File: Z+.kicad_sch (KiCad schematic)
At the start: 8 parts

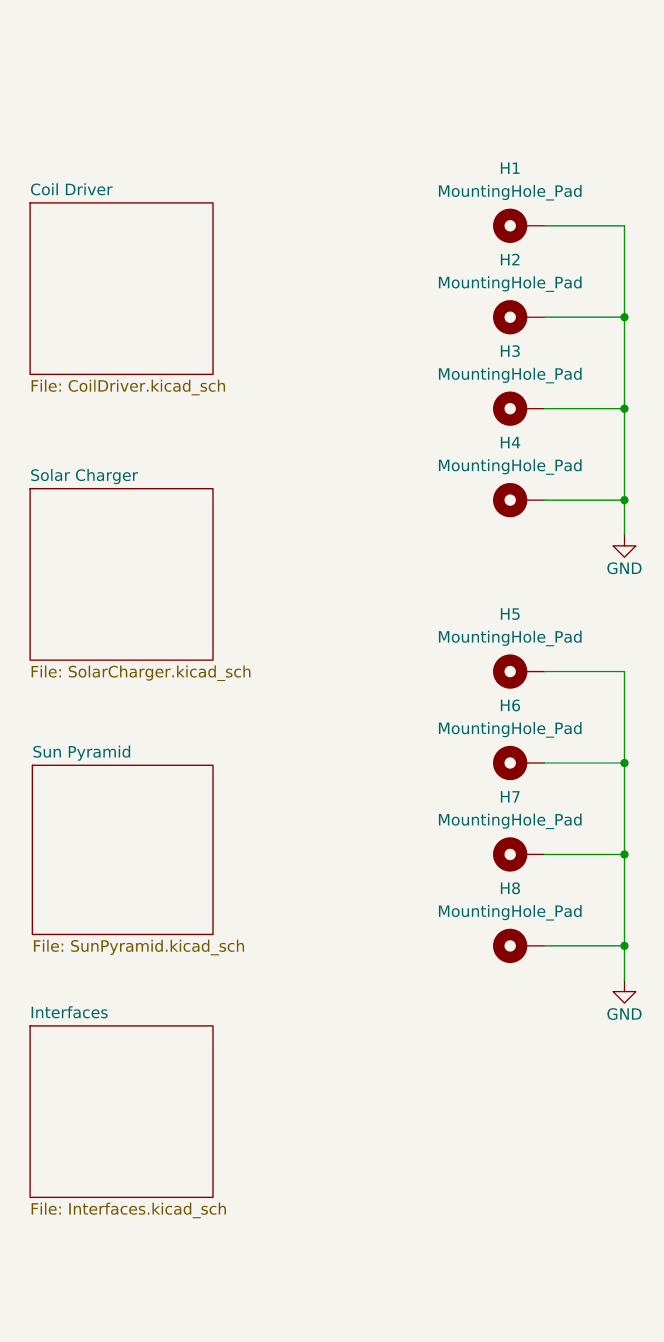
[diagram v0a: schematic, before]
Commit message: Cleaned up silkscreen
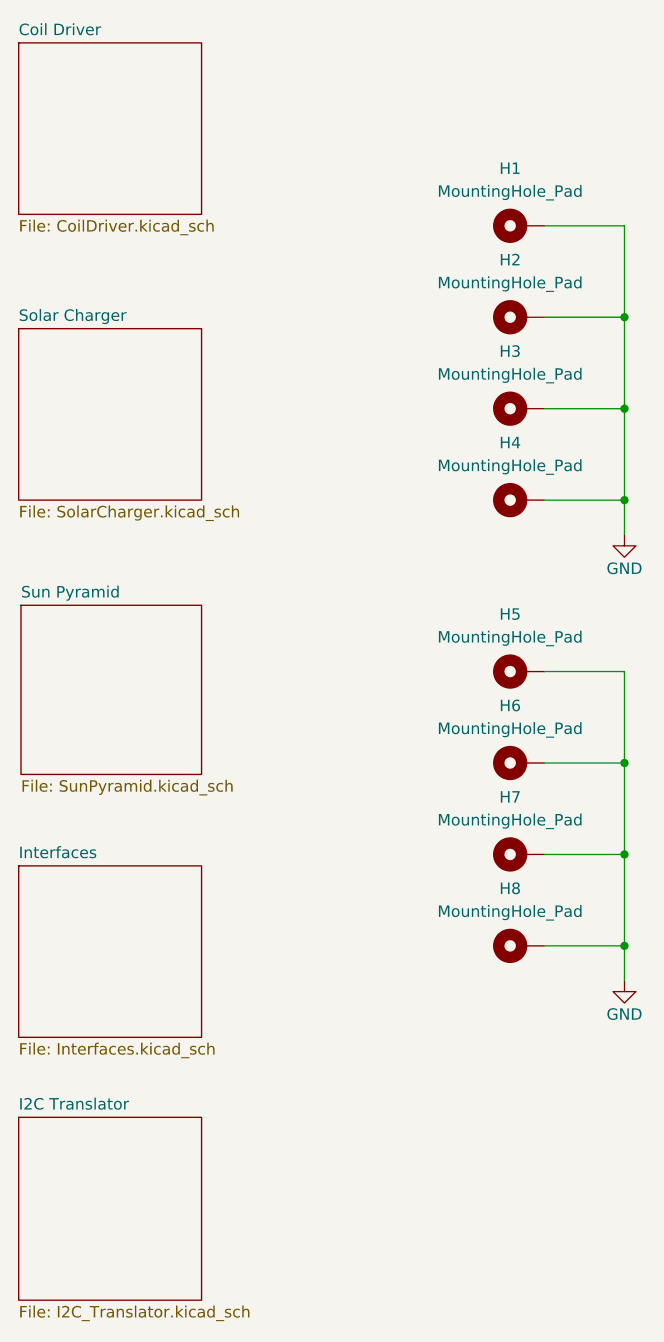
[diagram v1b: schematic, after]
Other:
- added sheet I2C Translator (I2C_Translator.kicad_sch)
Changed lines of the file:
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@@
 	)
 	(sheet
-		(at 107.95 73.66)
+		(at 106.68 55.88)
 		(size 20.32 19.05)
 		(fields_autoplaced yes)
@@
 		)
 		(property "Sheetname" "Solar Charger"
-			(at 107.95 72.9484 0)
+			(at 106.68 55.1684 0)
 			(effects
 				(font
@@
 		)
 		(property "Sheetfile" "SolarCharger.kicad_sch"
-			(at 107.95 93.2946 0)
+			(at 106.68 75.5146 0)
 			(effects
 				(font
@@
 	)
 	(sheet
-		(at 108.204 104.394)
+		(at 106.934 86.614)
 		(size 20.066 18.796)
 		(fields_autoplaced yes)
@@
 		)
 		(property "Sheetname" "Sun Pyramid"
-			(at 108.204 103.6824 0)
+			(at 106.934 85.9024 0)
 			(effects
 				(font
@@
 		)
 		(property "Sheetfile" "SunPyramid.kicad_sch"
-			(at 108.204 123.7746 0)
+			(at 106.934 105.9946 0)
 			(effects
 				(font
@@
 	)
 	(sheet
-		(at 107.95 133.35)
+		(at 106.68 143.51)
+		(size 20.32 20.32)
+		(fields_autoplaced yes)
+		(stroke
+			(width 0.1524)
+			(type solid)
+		)
+		(fill
+			(color 0 0 0 0.0000)
+		)
+		(property "Sheetname" "I2C Translator"
+			(at 106.68 142.7984 0)
+			(effects
+				(font
+					(size 1.27 1.27)
+				)
+				(justify left bottom)
+			)
+		)
+		(property "Sheetfile" "I2C_Translator.kicad_sch"
+			(at 106.68 164.4146 0)
+			(effects
+				(font
+					(size 1.27 1.27)
+				)
+				(justify left top)
+			)
+		)
+		(instances
+			(project "Z+"
+				(path "/977a45af-b6d4-4b54-8e70-e74e2c44e8e7"
+					(page "23")
+				)
+			)
+		)
+	)
+	(sheet
+		(at 106.68 115.57)
 		(size 20.32 19.05)
 		(fields_autoplaced yes)
@@
 		)
 		(property "Sheetname" "Interfaces"
-			(at 107.95 132.6384 0)
+			(at 106.68 114.8584 0)
 			(effects
 				(font
@@
 		)
 		(property "Sheetfile" "Interfaces.kicad_sch"
-			(at 107.95 152.9846 0)
+			(at 106.68 135.2046 0)
 			(effects
 				(font
@@
 	)
 	(sheet
-		(at 107.95 41.91)
+		(at 106.68 24.13)
 		(size 20.32 19.05)
 		(fields_autoplaced yes)
@@
 		)
 		(property "Sheetname" "Coil Driver"
-			(at 107.95 41.1984 0)
+			(at 106.68 23.4184 0)
 			(effects
 				(font
@@
 		)
 		(property "Sheetfile" "CoilDriver.kicad_sch"
-			(at 107.95 61.5446 0)
+			(at 106.68 43.7646 0)
 			(effects
 				(font
